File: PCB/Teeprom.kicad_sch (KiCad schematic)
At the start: 3 parts, among them J1 Tandy_100_102_200_option_rom, U1 28C256 / FM18W08

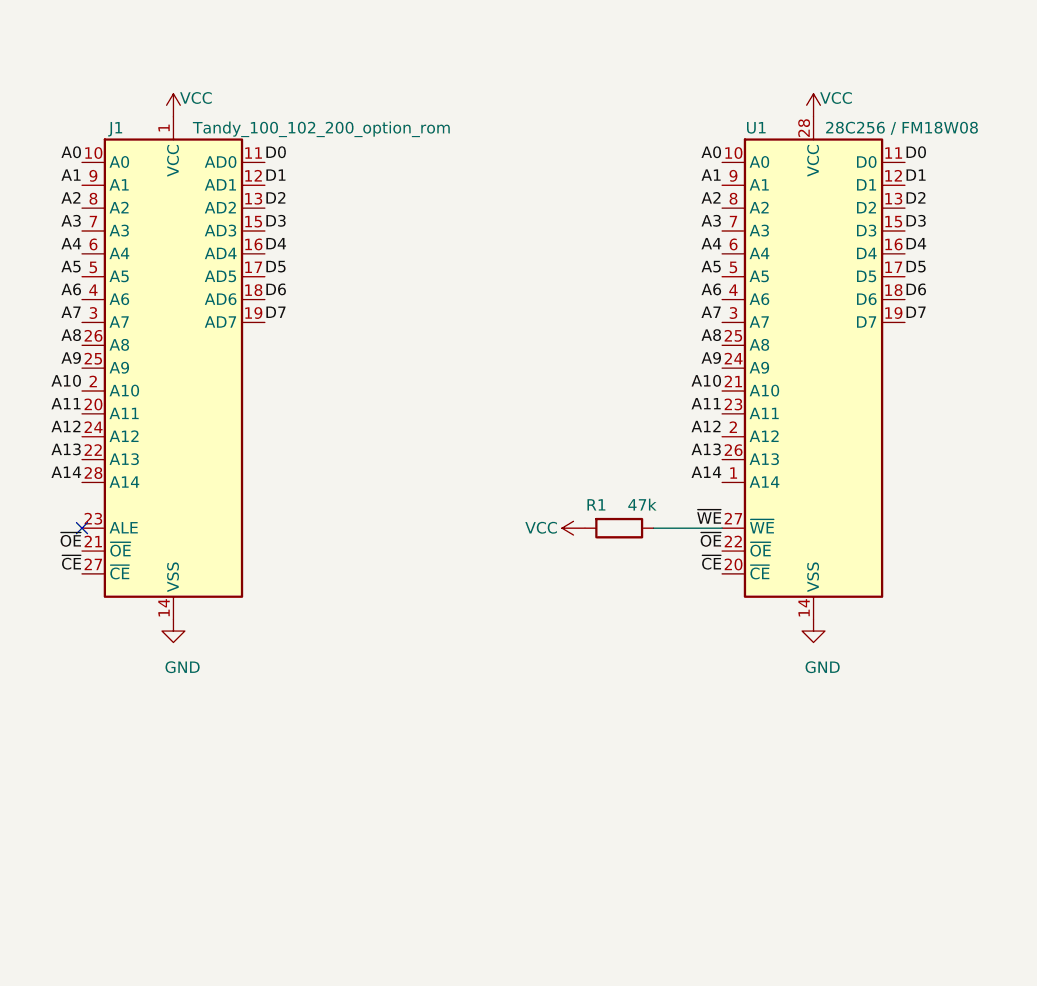
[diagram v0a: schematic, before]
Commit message: add caps & fiducials, remove dead shapeways links
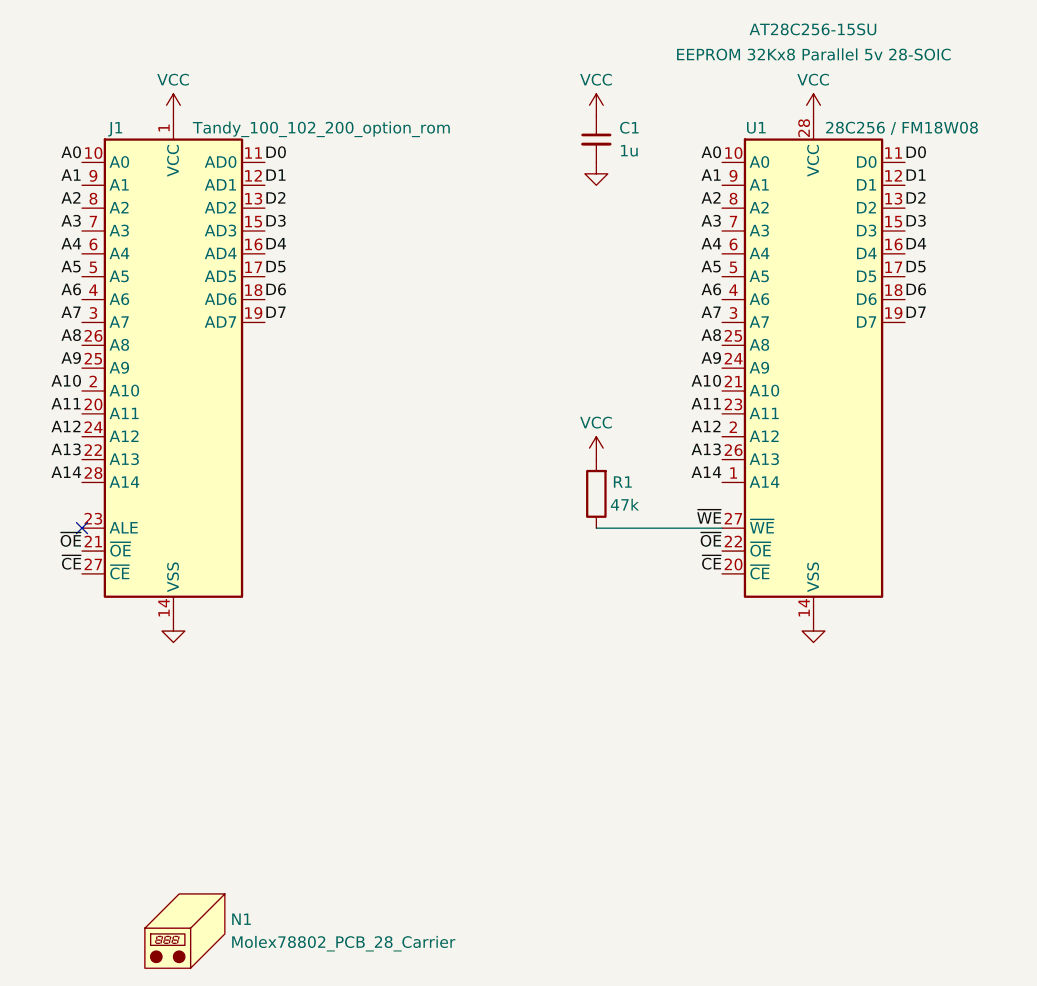
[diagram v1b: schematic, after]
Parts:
- added C1: 1u, 000_LOCAL:C_0805, symbol 000_LOCAL:C
- added N1: Molex78802_PCB_28_Carrier, 000_LOCAL:Molex78802_PCB_28_Carrier, symbol 000_LOCAL:Housing
- J1: now left out of the parts list
- R1: MPN (none) -> CRCW080547K0FKEA
- U1: MPN (none) -> AT28C256-15SU
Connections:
- net GND: now also C1.2
- net VCC: now also C1.1
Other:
- moved on the sheet: R1
